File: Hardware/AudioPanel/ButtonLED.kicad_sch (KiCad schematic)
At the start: 6 parts, among them U19 WS2811

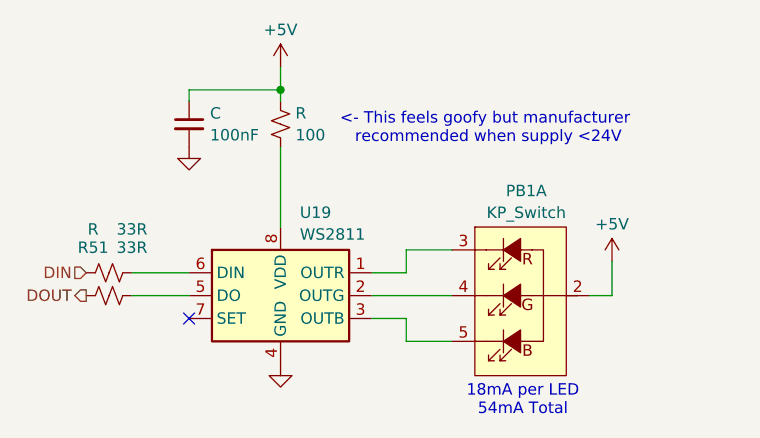
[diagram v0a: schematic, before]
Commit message: Fixed undefined LED_IN net
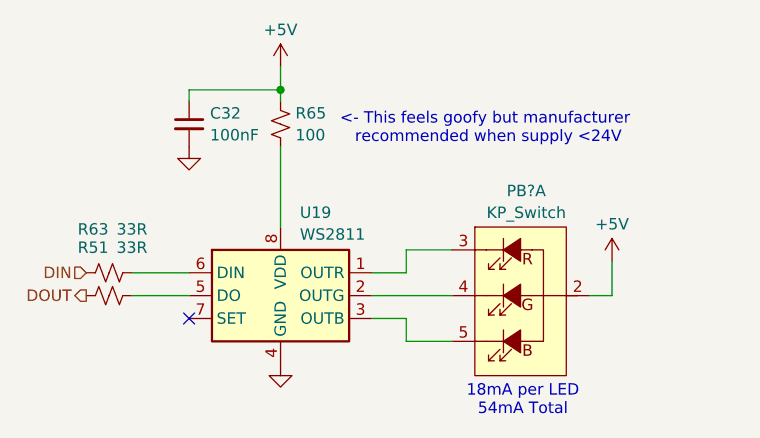
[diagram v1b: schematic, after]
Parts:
- renumbered C to C32, PB1 to PB?, R to R63, R to R65
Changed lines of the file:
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@@
 		(dnp no)
 		(fields_autoplaced yes)
-		(property "Reference" "C"
+		(property "Reference" "C?"
 			(at 131.8641 71.1841 0)
 			(effects
@@
 				(path "/2de36a1b-eee5-458c-8325-256a7162eff5/a5cce8a2-fa1f-45df-8605-c295d18be7f1/087c1b72-25ed-41f0-acdd-4665839c97ce"
 					(reference "C32")
+					(unit 1)
+				)
+				(path "/2de36a1b-eee5-458c-8325-256a7162eff5/a5cce8a2-fa1f-45df-8605-c295d18be7f1/0d672bb0-5c3c-47db-9d26-ada4d5a94edf"
+					(reference "C?")
 					(unit 1)
 				)
@@
 		(dnp no)
 		(fields_autoplaced yes)
-		(property "Reference" "PB1"
+		(property "Reference" "PB?"
 			(at 167.005 79.8025 0)
 			(effects
@@
 		)
 		(pin "1"
+		)
+		(instances
+			(project "PilotAudioPanel"
+				(path "/2de36a1b-eee5-458c-8325-256a7162eff5/a5cce8a2-fa1f-45df-8605-c295d18be7f1/087c1b72-25ed-41f0-acdd-4665839c97ce"
+					(reference "PB?")
+					(unit 1)
+				)
+				(path "/2de36a1b-eee5-458c-8325-256a7162eff5/a5cce8a2-fa1f-45df-8605-c295d18be7f1/0d672bb0-5c3c-47db-9d26-ada4d5a94edf"
+					(reference "PB?")
+					(unit 1)
+				)
+				(path "/2de36a1b-eee5-458c-8325-256a7162eff5/a5cce8a2-fa1f-45df-8605-c295d18be7f1/12425dc7-ab06-4bff-804a-d650a7ab7f2f"
+					(reference "PB?")
+					(unit 1)
+				)
+				(path "/2de36a1b-eee5-458c-8325-256a7162eff5/a5cce8a2-fa1f-45df-8605-c295d18be7f1/390c3102-f6c6-464a-abca-49d3743e5737"
+					(reference "PB?")
+					(unit 1)
+				)
+				(path "/2de36a1b-eee5-458c-8325-256a7162eff5/a5cce8a2-fa1f-45df-8605-c295d18be7f1/3c1c4f7e-9d2a-4715-83bc-474e02a2363b"
+					(reference "PB?")
+					(unit 1)
+				)
+				(path "/2de36a1b-eee5-458c-8325-256a7162eff5/a5cce8a2-fa1f-45df-8605-c295d18be7f1/45f10693-960d-407b-bcdb-44cffc888f0e"
+					(reference "PB?")
+					(unit 1)
+				)
+				(path "/2de36a1b-eee5-458c-8325-256a7162eff5/a5cce8a2-fa1f-45df-8605-c295d18be7f1/511f6806-7072-4fc6-ba0e-840605abf478"
+					(reference "PB?")
+					(unit 1)
+				)
+				(path "/2de36a1b-eee5-458c-8325-256a7162eff5/a5cce8a2-fa1f-45df-8605-c295d18be7f1/5c9bf123-f1c8-4a1f-b808-ac6ee42c4937"
+					(reference "PB?")
+					(unit 1)
+				)
+				(path "/2de36a1b-eee5-458c-8325-256a7162eff5/a5cce8a2-fa1f-45df-8605-c295d18be7f1/954c0d67-c94b-4af7-816f-200e052b64c9"
+					(reference "PB?")
+					(unit 1)
+				)
+				(path "/2de36a1b-eee5-458c-8325-256a7162eff5/a5cce8a2-fa1f-45df-8605-c295d18be7f1/d2501b73-7727-43e9-a80b-16f0f6fed20b"
+					(reference "PB?")
+					(unit 1)
+				)
+				(path "/2de36a1b-eee5-458c-8325-256a7162eff5/a5cce8a2-fa1f-45df-8605-c295d18be7f1/d7b85838-5187-411c-b5da-a623aecf8ad2"
+					(reference "PB?")
+					(unit 1)
+				)
+				(path "/2de36a1b-eee5-458c-8325-256a7162eff5/a5cce8a2-fa1f-45df-8605-c295d18be7f1/fb3ef425-4387-410f-8202-5f46898723c5"
+					(reference "PB?")
+					(unit 1)
+				)
+			)
 		)
 	)
@@
 		(on_board yes)
 		(dnp no)
-		(property "Reference" "R"
+		(property "Reference" "R?"
 			(at 118.872 84.074 90)
 			(effects
@@
 				(path "/2de36a1b-eee5-458c-8325-256a7162eff5/a5cce8a2-fa1f-45df-8605-c295d18be7f1/087c1b72-25ed-41f0-acdd-4665839c97ce"
 					(reference "R63")
+					(unit 1)
+				)
+				(path "/2de36a1b-eee5-458c-8325-256a7162eff5/a5cce8a2-fa1f-45df-8605-c295d18be7f1/0d672bb0-5c3c-47db-9d26-ada4d5a94edf"
+					(reference "R?")
 					(unit 1)
 				)
@@
 		(dnp no)
 		(fields_autoplaced yes)
-		(property "Reference" "#PWR"
+		(property "Reference" "#PWR?"
 			(at 139.7 69.85 0)
 			(effects
@@
 				(path "/2de36a1b-eee5-458c-8325-256a7162eff5/a5cce8a2-fa1f-45df-8605-c295d18be7f1/087c1b72-25ed-41f0-acdd-4665839c97ce"
 					(reference "#PWR079")
+					(unit 1)
+				)
+				(path "/2de36a1b-eee5-458c-8325-256a7162eff5/a5cce8a2-fa1f-45df-8605-c295d18be7f1/0d672bb0-5c3c-47db-9d26-ada4d5a94edf"
+					(reference "#PWR?")
 					(unit 1)
 				)
@@
 		(dnp no)
 		(fields_autoplaced yes)
-		(property "Reference" "#PWR"
+		(property "Reference" "#PWR?"
 			(at 129.54 81.28 0)
 			(effects
@@
 				(path "/2de36a1b-eee5-458c-8325-256a7162eff5/a5cce8a2-fa1f-45df-8605-c295d18be7f1/087c1b72-25ed-41f0-acdd-4665839c97ce"
 					(reference "#PWR078")
+					(unit 1)
+				)
+				(path "/2de36a1b-eee5-458c-8325-256a7162eff5/a5cce8a2-fa1f-45df-8605-c295d18be7f1/0d672bb0-5c3c-47db-9d26-ada4d5a94edf"
+					(reference "#PWR?")
 					(unit 1)
 				)
@@
 		(dnp no)
 		(fields_autoplaced yes)
-		(property "Reference" "R"
+		(property "Reference" "R?"
 			(at 141.351 71.1778 0)
 			(effects
@@
 					(unit 1)
 				)
+				(path "/2de36a1b-eee5-458c-8325-256a7162eff5/a5cce8a2-fa1f-45df-8605-c295d18be7f1/0d672bb0-5c3c-47db-9d26-ada4d5a94edf"
+					(reference "R?")
+					(unit 1)
+				)

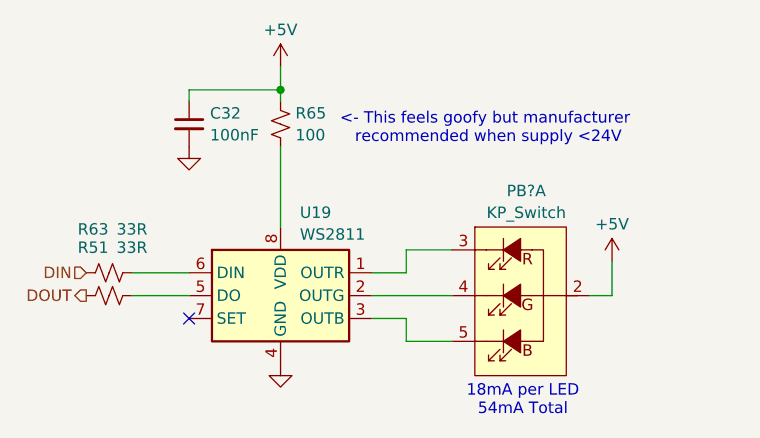
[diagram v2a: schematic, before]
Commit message: Added headphone and speaker jack interfaces
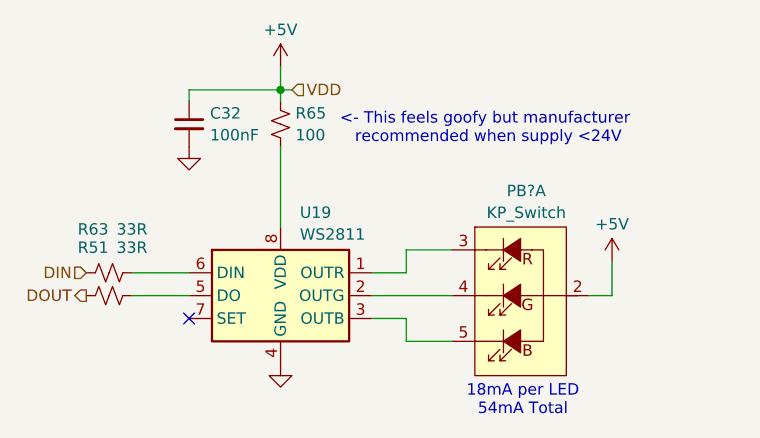
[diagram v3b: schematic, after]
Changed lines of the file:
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@@
+	(wire
+		(pts
+			(xy 139.7 68.58) (xy 140.97 68.58)
+		)
+		(stroke
+			(width 0)
+			(type default)
+		)
+	)
 	(wire
 		(pts
@@
 		)
 	)
+	(hierarchical_label "VDD"
+		(shape input)
+		(at 140.97 68.58 0)
+		(effects
+			(font
+				(size 1.27 1.27)
+			)
+			(justify left)
+		)
+	)

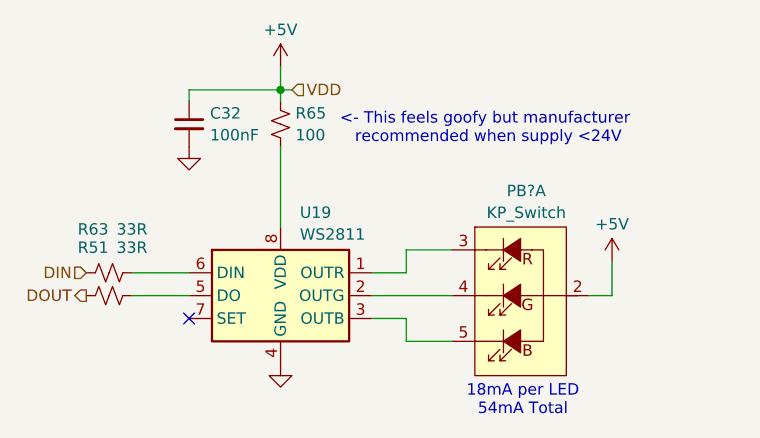
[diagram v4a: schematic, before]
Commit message: Realized that I need to rethink how I'm going to mix the radio audio with the stereo audio
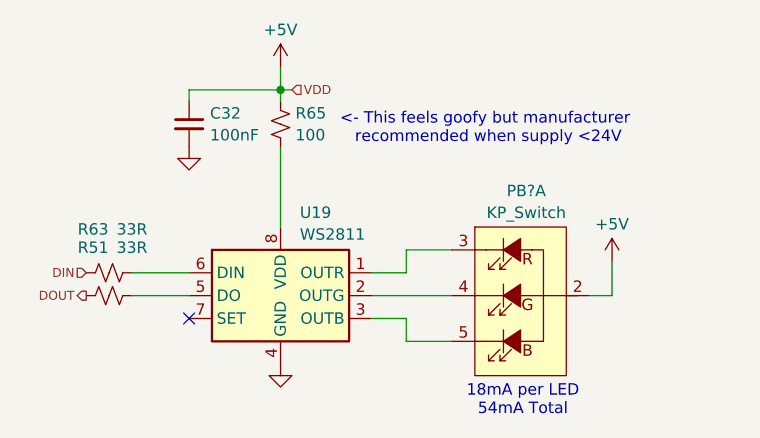
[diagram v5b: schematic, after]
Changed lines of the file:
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@@
 		(effects
 			(font
-				(size 1.27 1.27)
+				(size 1 1)
 			)
 			(justify left)
@@
 		(effects
 			(font
-				(size 1.27 1.27)
+				(size 1 1)
 				(color 105 14 0 1)
 			)
@@
 		(effects
 			(font
-				(size 1.27 1.27)
+				(size 1 1)
 				(color 105 14 0 1)
 			)

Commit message: Cleaned up sheet voltage inputs
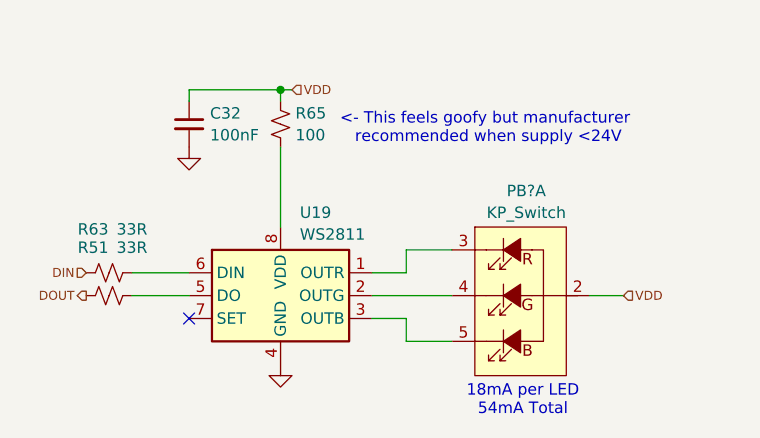
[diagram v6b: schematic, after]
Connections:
- net +5V renamed VDD
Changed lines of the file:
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@@
-	(wire
-		(pts
-			(xy 139.7 66.04) (xy 139.7 68.58)
-		)
-		(stroke
-			(width 0)
-			(type default)
-		)
-	)
 	(wire
 		(pts
@@
 	(wire
 		(pts
-			(xy 176.53 87.63) (xy 176.53 91.44)
-		)
-		(stroke
-			(width 0)
-			(type default)
-		)
-	)
-	(wire
-		(pts
 			(xy 149.86 91.44) (xy 158.75 91.44)
 		)
@@
 	(wire
 		(pts
-			(xy 176.53 91.44) (xy 173.99 91.44)
+			(xy 173.99 91.44) (xy 177.8 91.44)
 		)
 		(stroke
@@
 		(shape input)
 		(at 140.97 68.58 0)
+		(effects
+			(font
+				(size 1 1)
+			)
+			(justify left)
+		)
+	)
+	(hierarchical_label "VDD"
+		(shape input)
+		(at 177.8 91.44 0)
 		(effects
 			(font
@@
 	)
 	(symbol
-		(lib_id "power:+5V")
-		(at 139.7 66.04 0)
-		(unit 1)
-		(exclude_from_sim no)
-		(in_bom yes)
-		(on_board yes)
-		(dnp no)
-		(fields_autoplaced yes)
-		(property "Reference" "#PWR?"
-			(at 139.7 69.85 0)
-			(effects
-				(font
-					(size 1.27 1.27)
-				)
-				(hide yes)
-			)
-		)
-		(property "Value" "+5V"
-			(at 139.7 61.9069 0)
-			(effects
-				(font
-					(size 1.27 1.27)
-				)
-			)
-		)
-		(property "Footprint" ""
-			(at 139.7 66.04 0)
-			(effects
-				(font
-					(size 1.27 1.27)
-				)
-				(hide yes)
-			)
-		)
-		(property "Datasheet" ""
-			(at 139.7 66.04 0)
-			(effects
-				(font
-					(size 1.27 1.27)
-				)
-				(hide yes)
-			)
-		)
-		(property "Description" "Power symbol creates a global label with name \"+5V\""
-			(at 139.7 66.04 0)
-			(effects
-				(font
-					(size 1.27 1.27)
-				)
-				(hide yes)
-			)
-		)
-		(pin "1"
-		)
-		(instances
-			(project "PilotAudioPanel"
-				(path "/2de36a1b-eee5-458c-8325-256a7162eff5/a5cce8a2-fa1f-45df-8605-c295d18be7f1/087c1b72-25ed-41f0-acdd-4665839c97ce"
-					(reference "#PWR079")
-					(unit 1)
-				)
-				(path "/2de36a1b-eee5-458c-8325-256a7162eff5/a5cce8a2-fa1f-45df-8605-c295d18be7f1/0d672bb0-5c3c-47db-9d26-ada4d5a94edf"
-					(reference "#PWR?")
-					(unit 1)
-				)
-				(path "/2de36a1b-eee5-458c-8325-256a7162eff5/a5cce8a2-fa1f-45df-8605-c295d18be7f1/12425dc7-ab06-4bff-804a-d650a7ab7f2f"
-					(reference "#PWR095")
-					(unit 1)
-				)
-				(path "/2de36a1b-eee5-458c-8325-256a7162eff5/a5cce8a2-fa1f-45df-8605-c295d18be7f1/390c3102-f6c6-464a-abca-49d3743e5737"
-					(reference "#PWR091")
-					(unit 1)
-				)
-				(path "/2de36a1b-eee5-458c-8325-256a7162eff5/a5cce8a2-fa1f-45df-8605-c295d18be7f1/3c1c4f7e-9d2a-4715-83bc-474e02a2363b"
-					(reference "#PWR071")
-					(unit 1)
-				)
-				(path "/2de36a1b-eee5-458c-8325-256a7162eff5/a5cce8a2-fa1f-45df-8605-c295d18be7f1/45f10693-960d-407b-bcdb-44cffc888f0e"
-					(reference "#PWR099")
-					(unit 1)
-				)
-				(path "/2de36a1b-eee5-458c-8325-256a7162eff5/a5cce8a2-fa1f-45df-8605-c295d18be7f1/511f6806-7072-4fc6-ba0e-840605abf478"
-					(reference "#PWR083")
-					(unit 1)
-				)
-				(path "/2de36a1b-eee5-458c-8325-256a7162eff5/a5cce8a2-fa1f-45df-8605-c295d18be7f1/5c9bf123-f1c8-4a1f-b808-ac6ee42c4937"
-					(reference "#PWR068")
-					(unit 1)
-				)
-				(path "/2de36a1b-eee5-458c-8325-256a7162eff5/a5cce8a2-fa1f-45df-8605-c295d18be7f1/954c0d67-c94b-4af7-816f-200e052b64c9"
-					(reference "#PWR087")
-					(unit 1)
-				)
-				(path "/2de36a1b-eee5-458c-8325-256a7162eff5/a5cce8a2-fa1f-45df-8605-c295d18be7f1/d2501b73-7727-43e9-a80b-16f0f6fed20b"
-					(reference "#PWR0103")
-					(unit 1)
-				)
-				(path "/2de36a1b-eee5-458c-8325-256a7162eff5/a5cce8a2-fa1f-45df-8605-c295d18be7f1/d7b85838-5187-411c-b5da-a623aecf8ad2"
-					(reference "#PWR075")
-					(unit 1)
-				)
-				(path "/2de36a1b-eee5-458c-8325-256a7162eff5/a5cce8a2-fa1f-45df-8605-c295d18be7f1/fb3ef425-4387-410f-8202-5f46898723c5"
-					(reference "#PWR0107")
-					(unit 1)
-				)
-			)
-		)
-	)
-	(symbol
 		(lib_id "Device:R_Small_US")
 		(at 120.65 91.44 90)
@@
 					(unit 1)
 				)
-			)
-		)
-	)
-	(symbol
-		(lib_id "power:+5V")
-		(at 176.53 87.63 0)
-		(unit 1)
-		(exclude_from_sim no)
-		(in_bom yes)
-		(on_board yes)
-		(dnp no)
-		(fields_autoplaced yes)
-		(property "Reference" "#PWR064"
-			(at 176.53 91.44 0)
-			(effects
-				(font
-					(size 1.27 1.27)
-				)
-				(hide yes)
-			)
-		)
-		(property "Value" "+5V"
-			(at 176.53 83.4969 0)
-			(effects
-				(font
-					(size 1.27 1.27)
-				)
-			)
-		)
-		(property "Footprint" ""
-			(at 176.53 87.63 0)
-			(effects
-				(font
-					(size 1.27 1.27)
-				)
-				(hide yes)
-			)
-		)
-		(property "Datasheet" ""
-			(at 176.53 87.63 0)
-			(effects
-				(font
-					(size 1.27 1.27)
-				)
-				(hide yes)
-			)
-		)
-		(property "Description" "Power symbol creates a global label with name \"+5V\""
-			(at 176.53 87.63 0)
-			(effects
-				(font
-					(size 1.27 1.27)
-				)
-				(hide yes)
-			)
-		)
-		(pin "1"
-		)
-		(instances
-			(project "PilotAudioPanel"
-				(path "/2de36a1b-eee5-458c-8325-256a7162eff5/a5cce8a2-fa1f-45df-8605-c295d18be7f1/087c1b72-25ed-41f0-acdd-4665839c97ce"
-					(reference "#PWR081")
-					(unit 1)
-				)
-				(path "/2de36a1b-eee5-458c-8325-256a7162eff5/a5cce8a2-fa1f-45df-8605-c295d18be7f1/0d672bb0-5c3c-47db-9d26-ada4d5a94edf"
-					(reference "#PWR064")
-					(unit 1)
-				)
-				(path "/2de36a1b-eee5-458c-8325-256a7162eff5/a5cce8a2-fa1f-45df-8605-c295d18be7f1/12425dc7-ab06-4bff-804a-d650a7ab7f2f"
-					(reference "#PWR097")
-					(unit 1)
-				)
-				(path "/2de36a1b-eee5-458c-8325-256a7162eff5/a5cce8a2-fa1f-45df-8605-c295d18be7f1/390c3102-f6c6-464a-abca-49d3743e5737"
-					(reference "#PWR093")
-					(unit 1)
-				)
-				(path "/2de36a1b-eee5-458c-8325-256a7162eff5/a5cce8a2-fa1f-45df-8605-c295d18be7f1/3c1c4f7e-9d2a-4715-83bc-474e02a2363b"
-					(reference "#PWR073")
-					(unit 1)
-				)
-				(path "/2de36a1b-eee5-458c-8325-256a7162eff5/a5cce8a2-fa1f-45df-8605-c295d18be7f1/45f10693-960d-407b-bcdb-44cffc888f0e"
-					(reference "#PWR0101")
-					(unit 1)
-				)
-				(path "/2de36a1b-eee5-458c-8325-256a7162eff5/a5cce8a2-fa1f-45df-8605-c295d18be7f1/511f6806-7072-4fc6-ba0e-840605abf478"
-					(reference "#PWR085")
-					(unit 1)
-				)
-				(path "/2de36a1b-eee5-458c-8325-256a7162eff5/a5cce8a2-fa1f-45df-8605-c295d18be7f1/5c9bf123-f1c8-4a1f-b808-ac6ee42c4937"
-					(reference "#PWR069")
-					(unit 1)
-				)
-				(path "/2de36a1b-eee5-458c-8325-256a7162eff5/a5cce8a2-fa1f-45df-8605-c295d18be7f1/954c0d67-c94b-4af7-816f-200e052b64c9"
-					(reference "#PWR089")
-					(unit 1)
-				)
-				(path "/2de36a1b-eee5-458c-8325-256a7162eff5/a5cce8a2-fa1f-45df-8605-c295d18be7f1/d2501b73-7727-43e9-a80b-16f0f6fed20b"
-					(reference "#PWR0105")
-					(unit 1)
-				)
-				(path "/2de36a1b-eee5-458c-8325-256a7162eff5/a5cce8a2-fa1f-45df-8605-c295d18be7f1/d7b85838-5187-411c-b5da-a623aecf8ad2"
-					(reference "#PWR077")
-					(unit 1)
-				)
-				(path "/2de36a1b-eee5-458c-8325-256a7162eff5/a5cce8a2-fa1f-45df-8605-c295d18be7f1/fb3ef425-4387-410f-8202-5f46898723c5"
-					(reference "#PWR0109")
-					(unit 1)
-				)
